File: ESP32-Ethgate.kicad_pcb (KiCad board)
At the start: 2 copper layers, 58 parts, among them J1 USB_B_Micro, J2 RJ45_Amphenol_RJMG1BD3B8K1ANR, Q1 UMH3N, SW1 RESET, SW2 PROG, U1 AMS1117-3.3, U2 ESP32-WROOM-32U, U3 CH340C, U4 W5500, Y1 25MHz

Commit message: finished layout
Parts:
- removed C17: 22n, Capacitor_SMD:C_0603_1608Metric
- removed C18, C19, C20, C21, C22, C23: 100n, Capacitor_SMD:C_0603_1608Metric
- removed R4: 0R, Resistor_SMD:R_0603_1608Metric
- removed SW1: RESET, Button_Switch_SMD:SW_SPST_CK_RS282G05A3
- removed SW2: PROG, Button_Switch_SMD:SW_SPST_CK_RS282G05A3
- removed Y1: 25MHz, Crystal:Crystal_SMD_3225-4Pin_3.2x2.5mm_HandSoldering
- added R22: 49K9, Resistor_SMD:R_0603_1608Metric, B.Cu at (90.9, 90.9)
- added R23: 0R, Resistor_SMD:R_0603_1608Metric, B.Cu at (74.0, 75.9)
- added R8: 10K, Resistor_SMD:R_0603_1608Metric, B.Cu at (108.8, 96.5)
- added U5: LAN8720A, Package_DFN_QFN:QFN-24-1EP_4x4mm_P0.5mm_EP2.6x2.6mm, B.Cu at (107.3, 88.0)
- C1, C2: value 100nF -> 100n; moved to B.Cu
- C10: value 22u -> 100n; footprint Capacitor_SMD:C_0805_2012Metric -> Capacitor_SMD:C_0603_1608Metric; moved to B.Cu
- C11: value 100n -> 1u1R; moved to B.Cu
- C12: value 4.7u -> 10n; footprint Capacitor_SMD:C_0805_2012Metric -> Capacitor_SMD:C_0603_1608Metric; moved to B.Cu
- C13: value 10n -> 470p; moved to B.Cu
- C14: value 10n -> 22n; moved to B.Cu
- C15: value 6.8n -> 10n; moved to B.Cu
- C16: value 6.8n -> 22n; moved to B.Cu
- C3, C4, C5, C6, C7, D1, F1, Q1, R1, R17, R18, R2, R5, U1, U3: moved to B.Cu
- C8, C9: value 18p -> 100n; moved to B.Cu
- FB1: value 120R@100MHz -> 30R; footprint Inductor_SMD:L_0603_1608Metric_Pad1.05x0.95mm_HandSolder -> Inductor_SMD:L_0603_1608Metric; moved to B.Cu
- J2: value RJ45_Amphenol_RJMG1BD3B8K1ANR -> HR911105A; footprint Connector_RJ:RJ45_Amphenol_RJMG1BD3B8K1ANR -> Connector_RJ:RJ45_Hanrun_HR911105A
- R10: value 10K -> 1K5; moved to B.Cu
- R11, R14: value 49R9 -> 10R; moved to B.Cu
- R12, R15: value 49R9 -> 33R; moved to B.Cu
- R13: value 12K4 1% -> 33R; moved to B.Cu
- R16, R20, R21: value 10K -> 49K9; moved to B.Cu
- R19: value 0R -> 12K1; moved to B.Cu
- R6: value 1M -> 10R; moved to B.Cu
- R9: value 10K -> 10R; moved to B.Cu
- U4: value W5500 -> 50MHz; footprint Package_QFP:LQFP-48_7x7mm_P0.5mm -> Oscillator:Oscillator_SMD_Abracon_ASDMB-4Pin_2.5x2.0mm; moved to B.Cu
- moved R3 110.1 mm to (74.1, 77.5)
- moved R21 108.2 mm to (90.9, 83.4), turned to 180 degrees
- moved R17 105.6 mm to (90.9, 93.1), turned to 180 degrees
- moved R18 104.9 mm to (90.9, 94.7), turned to 180 degrees
- moved R20 104.7 mm to (90.9, 86.5), turned to 180 degrees
- moved D2 102.0 mm to (69.8, 77.5)
- moved D3 101.4 mm to (70.1, 62.9)
- moved C3 96.5 mm to (85.2, 65.0), turned to 90 degrees
- moved R16 95.9 mm to (90.9, 88.3), turned to 180 degrees
- moved C16 93.9 mm to (90.9, 81.5)
- moved R7 91.8 mm to (74.5, 63.5)
- moved C4 91.0 mm to (98.7, 73.8), turned to 270 degrees
- moved C15 89.1 mm to (105.5, 96.5), turned to 270 degrees
- moved C7 88.6 mm to (100.3, 63.4), turned to 180 degrees
- moved C6 88.1 mm to (91.1, 76.5)
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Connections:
- net SLED renamed /SLED
- C1 pad 1: +3V3 -> GND
- C1 pad 2: GND -> +3V3
- C11 pad 1: +3V3 -> /VDDCR
- C12 pad 1: GND -> +3.3VA
- C12 pad 2: Net-(C12-Pad2) -> GND
- C13 pad 1: GND -> /VDDCR
- C13 pad 2: Net-(C13-Pad2) -> GND
- C14 pad 1: Net-(C14-Pad1) -> +3.3VA
- C15 pad 1: Net-(C15-Pad1) -> +3.3VA
- C15 pad 2: /RXN -> GND
- C16 pad 1: Net-(C16-Pad1) -> +3.3VA
- C16 pad 2: /RXP -> GND
- C2 pad 1: +3V3 -> /EN
- C8 pad 1: /XI -> +3V3
- C9 pad 1: /XO -> /nRST
- J1 pad 6: Net-(J1-Pad6) -> GND1
- R10 pad 1: Net-(R10-Pad1) -> +3V3
- R10 pad 2: +3V3 -> /MDIO
- R11 pad 1: +3.3VA -> /CRS_DV
- R11 pad 2: /TXP -> Net-(R11-Pad2)
- R12 pad 1: /RXN -> /IO0
- R12 pad 2: Net-(C14-Pad1) -> Net-(R12-Pad2)
- R13 pad 1: GND -> /IO0
- R13 pad 2: Net-(R13-Pad2) -> /CLOCK
- R14 pad 1: +3.3VA -> Net-(R14-Pad1)
- R14 pad 2: /TXP -> /RXD0
- R15 pad 1: /RXP -> /CLOCK
- R15 pad 2: Net-(C14-Pad1) -> /XTAL
- R16 pad 1: +3.3VA -> /RXP
- R16 pad 2: Net-(C17-Pad1) -> +3.3VA
- R17 pad 2: Net-(J2-PadL2) -> Net-(J2-Pad9)
- R18 pad 2: Net-(J2-PadL3) -> Net-(J2-Pad11)
- R19 pad 1: Net-(J2-Pad13) -> GND
- R19 pad 2: GND -> /RBIAS
- R20 pad 1: +3V3 -> /TXN
- R20 pad 2: /~SCS -> +3.3VA
- R21 pad 1: +3V3 -> /TXP
- R21 pad 2: /~WRST -> +3.3VA
- R5 pad 1: Net-(R5-Pad1) -> /PHY_PWR
- R5 pad 2: +3V3 -> GND
- R6 pad 1: /XO -> Net-(R6-Pad1)
- R6 pad 2: /XI -> +3V3
- R9 pad 2: +3V3 -> /RXD1
- U2 pad 10: /EN -> /RXD0
- U2 pad 11: /~WRST -> /RXD1
- U2 pad 12: (no net) -> /CRS_DV
- U2 pad 28: (no net) -> /PHY_PWR
- U2 pad 29: /~SCS -> (no net)
- U2 pad 30: /SCLK -> /MDIO
- U2 pad 31: /MISO -> /TXD0
- U2 pad 33: (no net) -> /TXEN
- U2 pad 36: (no net) -> /TXD1
- U2 pad 37: /MOSI -> /MDC
- U4 pad 1: /TXN -> /PHY_PWR
- U4 pad 2: /TXP -> GND
- U4 pad 3: GND -> /CLOCK
- U4 pad 4: +3.3VA -> +3V3
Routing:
- net +3V3: track 0.00 -> 163.0 mm, vias 0 -> 9
- net +3.3VA: track 0.00 -> 82.4 mm, vias 0 -> 7
- net /SLED: track 0.00 -> 65.6 mm, vias 0 -> 4
- net /eRX: track 0.00 -> 58.8 mm, vias 0 -> 1
- net /TXD1: track 0.00 -> 47.7 mm, vias 0 -> 3
- net /eTX: track 0.00 -> 46.6 mm, vias 0 -> 1
- net /TXEN: track 0.00 -> 39.8 mm, vias 0 -> 1
- net /TXD0: track 0.00 -> 39.3 mm, vias 0 -> 1
- net /MDC: track 0.00 -> 38.7 mm, vias 0 -> 1
- net Net-(J1-Pad2): track 0.00 -> 37.0 mm, vias 0 -> 1
- net /EN: track 0.00 -> 36.9 mm, vias 0 -> 2
- net Net-(J1-Pad3): track 0.00 -> 34.9 mm, vias 0 -> 1
- net /PHY_PWR: track 0.00 -> 34.9 mm, vias 0 -> 1
- net /IO0: track 0.00 -> 33.2 mm, vias 0 -> 1
- net +5V: track 0.00 -> 29.7 mm
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- added copper zone on B.Cu, net GND
- added copper zone on F.Cu, net GND
- added copper zone on B.Cu, net GND1
- added copper zone on F.Cu, net GND1
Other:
- board outline added: 76.2 x 38.1 mm
- net class Default: clearance 0.3 -> 0.26; via_dia 1.2 -> 1
- rule trace_clearance: 0.3 -> 0.26
- rule via_min_size: 1.2 -> 1
- board text added: "ESP32-Ethgate v1 cperiod 2021"

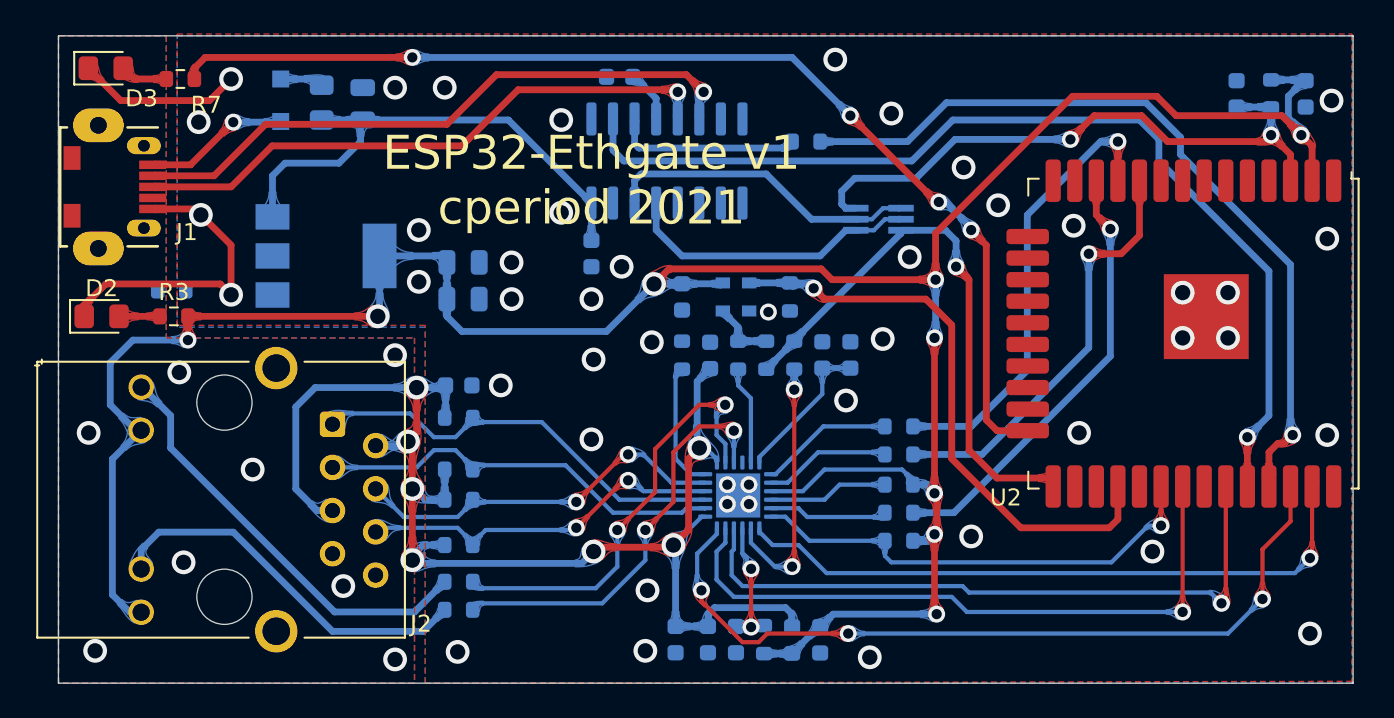
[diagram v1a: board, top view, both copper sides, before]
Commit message: add USB ESD, generate rounded tracks version
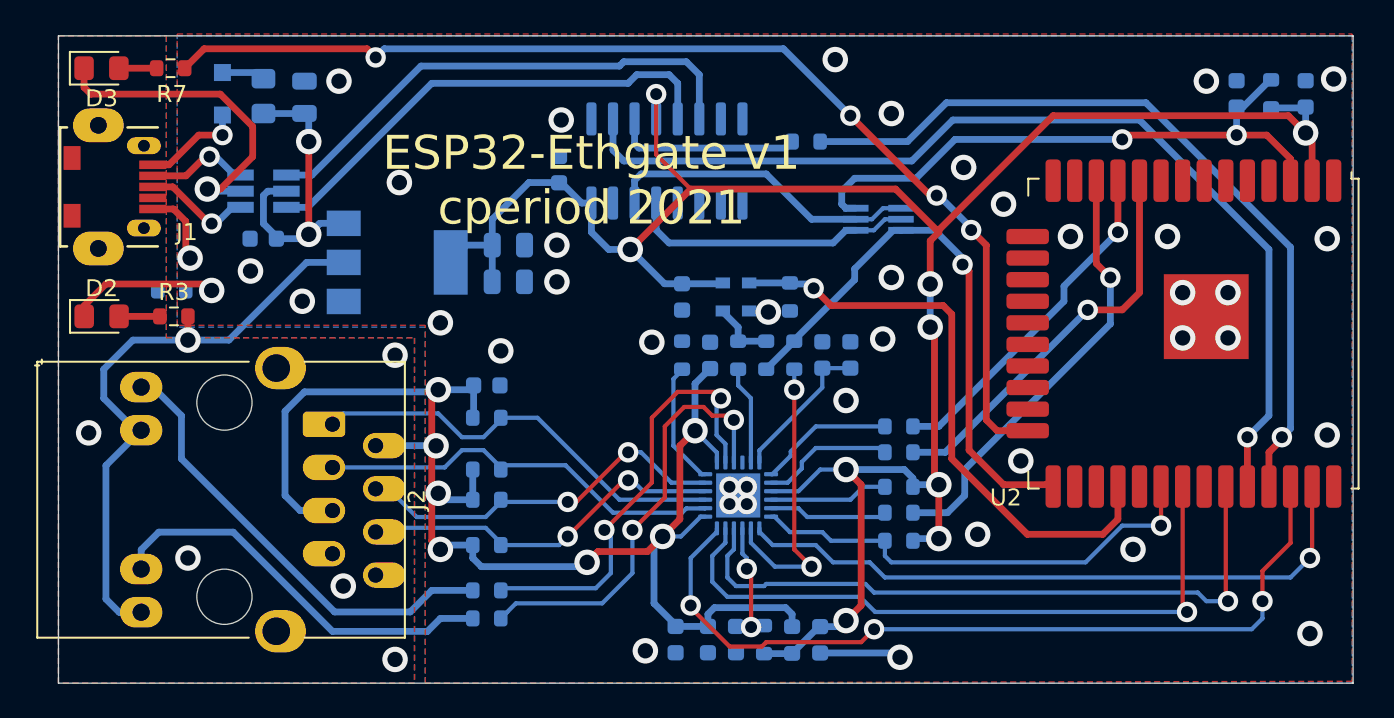
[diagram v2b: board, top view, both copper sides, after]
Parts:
- added U6: USBLC6-2SC6, Package_TO_SOT_SMD:SOT-23-6_Handsoldering, B.Cu at (79.4, 70.1)
- J2: footprint Connector_RJ:RJ45_Hanrun_HR911105A -> CPB:RJ45_Hanrun_HR911105A_Oval
- moved C7 23.0 mm to (79.4, 72.9)
- moved C4 5.29 mm to (96.8, 68.8), turned to 90 degrees
- moved U1 4.21 mm to (87.2, 74.3)
- moved C3 3.45 mm to (81.8, 64.6)
- moved D1 3.45 mm to (77.0, 64.4)
- moved F1 3.45 mm to (79.4, 64.5)
- moved C5 2.85 mm to (93.8, 73.3)
- moved C6 2.85 mm to (93.8, 75.4)
- moved R18 1.73 mm to (92.5, 95.2)
- moved R17 1.73 mm to (92.5, 93.6)
- moved C16 1.65 mm to (92.5, 81.5)
- moved R16 1.65 mm to (92.5, 88.3)
- moved R20 1.65 mm to (92.5, 86.5)
- moved R21 1.65 mm to (92.5, 83.4)
- moved R22 1.65 mm to (92.5, 90.9)
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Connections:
- C4 pad 1: +5V -> +3V3
- C7 pad 1: Net-(C7-Pad1) -> +5V
- U3 pad 16: +5V -> +3V3
- U3 pad 4: Net-(C7-Pad1) -> +3V3
- U3 pad 5: Net-(J1-Pad3) -> Net-(U3-Pad5)
- U3 pad 6: Net-(J1-Pad2) -> Net-(U3-Pad6)
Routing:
- net Net-(J1-Pad2): track 37.0 -> 6.19 mm
- net Net-(U3-Pad6): track 0.00 -> 30.0 mm
- net Net-(U3-Pad5): track 0.00 -> 28.6 mm
- net Net-(J1-Pad3): track 34.9 -> 6.51 mm
- net +5V: track 29.7 -> 19.2 mm, vias 0 -> 2
- net GND: track 28.2 -> 37.4 mm, vias 46 -> 41
- net /RXD1: track 27.2 -> 19.9 mm
- net +3V3: track 163.0 -> 167.7 mm, vias 9 -> 10
- net +3.3VA: track 82.4 -> 85.5 mm
- net Net-(C7-Pad1): track 3.11 -> 0.00 mm
- net Net-(D1-Pad2): track 8.59 -> 6.01 mm
- net Net-(J2-Pad9): track 25.2 -> 27.0 mm
- net /TXD1: track 47.7 -> 49.5 mm
- net /ACTLED: track 24.6 -> 26.2 mm
- net Net-(R12-Pad2): track 15.5 -> 17.0 mm
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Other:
- net class Default: via_dia 1 -> 1.2; via_drill 0.6 -> 0.7
- net class Power added: clearance 0.3, trace_width 0.4, via_dia 1.5, via_drill 0.9
- rule via_min_drill: 0.6 -> 0.7
- rule via_min_size: 1 -> 1.2

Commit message: more tweaks
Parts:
- R16, R20, R21, R22: value 49K9 -> 49R9
- R17, R18, R3, R7: value 1K -> 1K5

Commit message: better, but still not working.
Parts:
- added D4: GREEN, LED_SMD:LED_0603_1608Metric_Castellated, F.Cu at (89.7, 80.2)
- added R4: 10K, Resistor_SMD:R_0603_1608Metric, F.Cu at (98.8, 74.9)
- C1, C10, C11, C12, C13, C14, C15, C16, C2, C3, C4, C5, C6, C7, C9, D1, F1, FB1, Q1, R1, R10, R11, R14, R15, R16, R17, R18, R19, R2, R20, R21, R22, R23, R8, R9, U3, U5, U6: moved to F.Cu
- C8: value 100n -> 22u; footprint Capacitor_SMD:C_0603_1608Metric -> Capacitor_SMD:C_0805_2012Metric; moved to F.Cu
- D2, D3: footprint LED_SMD:LED_0805_2012Metric_Pad1.15x1.40mm_HandSolder -> LED_SMD:LED_0603_1608Metric_Castellated
- R12: value 33R -> 10K; moved to F.Cu
- R13: value 33R -> 1K5; moved to F.Cu
- R5: value 10K -> 1K5; moved to F.Cu
- R6: value 10R -> 1K5; moved to F.Cu
- U1: value AMS1117-3.3 -> HT7233; footprint Package_TO_SOT_SMD:SOT-223-3_TabPin2 -> Package_TO_SOT_SMD:SOT-23-5; moved to F.Cu
- U4: value 50MHz -> HT7233; footprint Oscillator:Oscillator_SMD_Abracon_ASDMB-4Pin_2.5x2.0mm -> Package_TO_SOT_SMD:SOT-23-5; moved to F.Cu
- moved R1 24.1 mm to (115.8, 71.8), turned to 0 degrees
- moved FB1 18.9 mm to (96.0, 84.4), turned to 270 degrees
- moved C10 18.3 mm to (105.3, 79.5), turned to 90 degrees
- moved R5 17.7 mm to (93.1, 80.2), turned to 0 degrees
- moved C9 17.0 mm to (106.9, 79.5), turned to 90 degrees
- moved R8 17.0 mm to (108.6, 79.5), turned to 90 degrees
- moved C11 15.8 mm to (110.1, 95.4), turned to 270 degrees
- moved C13 15.8 mm to (111.8, 95.4), turned to 270 degrees
- moved R15 15.6 mm to (107.8, 95.3), turned to 90 degrees
- moved C12 15.5 mm to (104.8, 95.3), turned to 270 degrees
- moved R19 15.5 mm to (103.1, 95.2), turned to 90 degrees
- moved C15 14.4 mm to (97.7, 84.4), turned to 90 degrees
- moved C14 12.8 mm to (99.4, 84.4), turned to 90 degrees
- moved C3 10.6 mm to (82.3, 75.1)
- moved D1 10.6 mm to (77.5, 74.9), turned to 90 degrees
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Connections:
- C10 pad 1: +3V3 -> /+3V3_LAN
- C8 pad 1: +3V3 -> /+3V3_LAN
- FB1 pad 1: +3V3 -> /+3V3_LAN
- J2 pad 10: +3V3 -> /+3V3_LAN
- J2 pad 12: +3V3 -> /+3V3_LAN
- R10 pad 1: +3V3 -> /+3V3_LAN
- R12 pad 1: /IO0 -> /+3V3_LAN
- R13 pad 1: /IO0 -> /+3V3_LAN
- R13 pad 2: /CLOCK -> /CRS_DV
- R15 pad 1: /CLOCK -> /PHY_CLK
- R5 pad 1: /PHY_PWR -> Net-(D4-Pad2)
- R5 pad 2: GND -> /+3V3_LAN
- R6 pad 2: +3V3 -> /+3V3_LAN
- R8 pad 2: +3V3 -> /+3V3_LAN
- U1 pad 1: GND -> +5V
- U1 pad 2: +3V3 -> GND
- U2 pad 14: (no net) -> /PHY_POWER
- U2 pad 28: /PHY_PWR -> /PHY_CLK
- U4 pad 1: /PHY_PWR -> +5V
- U4 pad 3: /CLOCK -> /PHY_POWER
- U4 pad 4: +3V3 -> (no net)
- U5 pad 9: +3V3 -> /+3V3_LAN
- U6 pad 1: Net-(J1-Pad3) -> Net-(J1-Pad2)
- U6 pad 3: Net-(J1-Pad2) -> Net-(J1-Pad3)
- U6 pad 4: Net-(U3-Pad6) -> Net-(U3-Pad5)
- U6 pad 6: Net-(U3-Pad5) -> Net-(U3-Pad6)
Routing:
- net /+3V3_LAN: track 0.00 -> 92.6 mm, vias 0 -> 5
- net +3V3: track 167.7 -> 109.5 mm, vias 10 -> 9
- net /PHY_POWER: track 0.00 -> 36.3 mm, vias 0 -> 2
- net /PHY_PWR: track 35.6 -> 0.00 mm, vias 1 -> 0
- net /PHY_CLK: track 0.00 -> 28.5 mm
- net Net-(U3-Pad6): track 30.0 -> 7.69 mm
- net Net-(U3-Pad5): track 28.6 -> 9.63 mm
- net +5V: track 19.2 -> 37.9 mm
- net GND: track 37.4 -> 55.5 mm, vias 41 -> 42
- net +3.3VA: track 85.5 -> 73.6 mm, vias 7 -> 4
- net /RXD1: track 19.9 -> 30.8 mm, vias 1 -> 2
- net /LINKLED: track 26.3 -> 15.9 mm
- net Net-(R12-Pad2): track 17.0 -> 6.65 mm, vias 2 -> 0
- net /TXN: track 24.3 -> 33.9 mm
- net /ACTLED: track 26.2 -> 17.7 mm
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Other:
- board text added: "ESP32-Ethgate v2 cperiod 2021"
- board text removed: "ESP32-Ethgate v1 cperiod 2021"

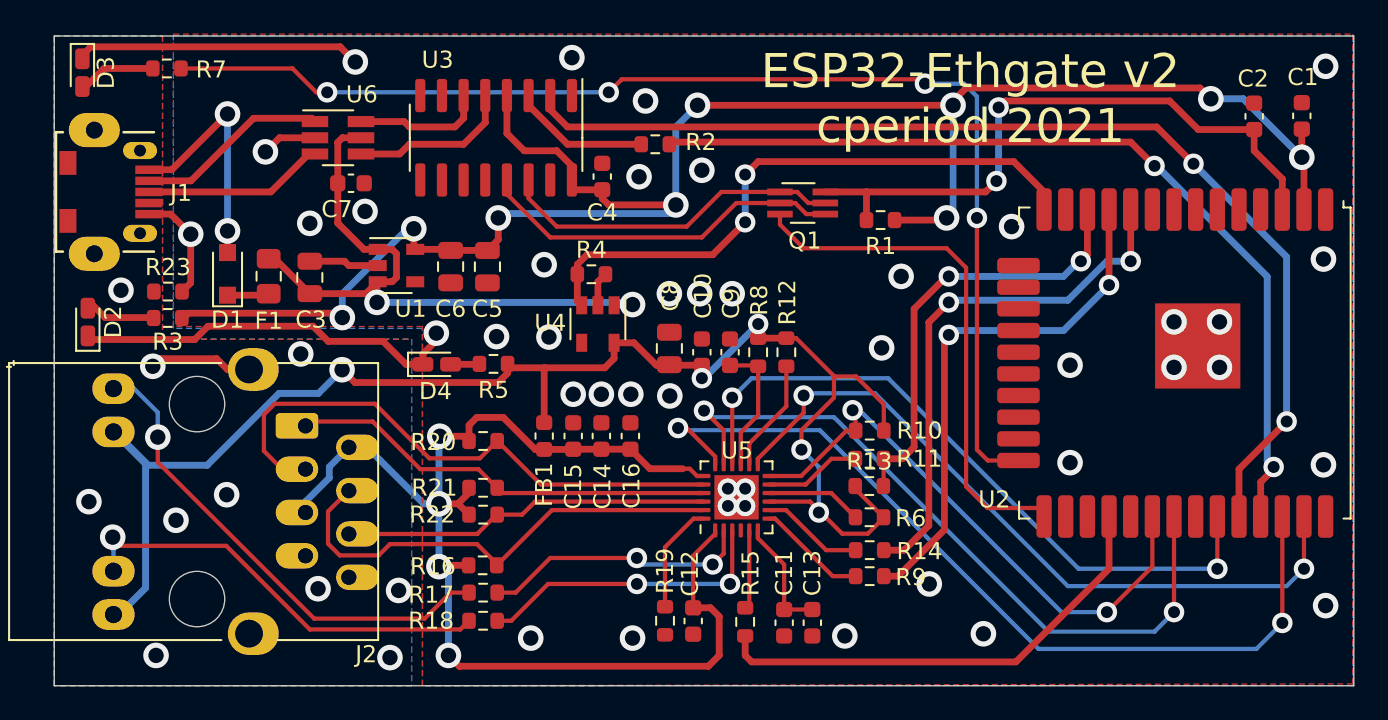
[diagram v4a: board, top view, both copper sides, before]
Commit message: some layout tweaks to clean things up and make assembly a hair easier
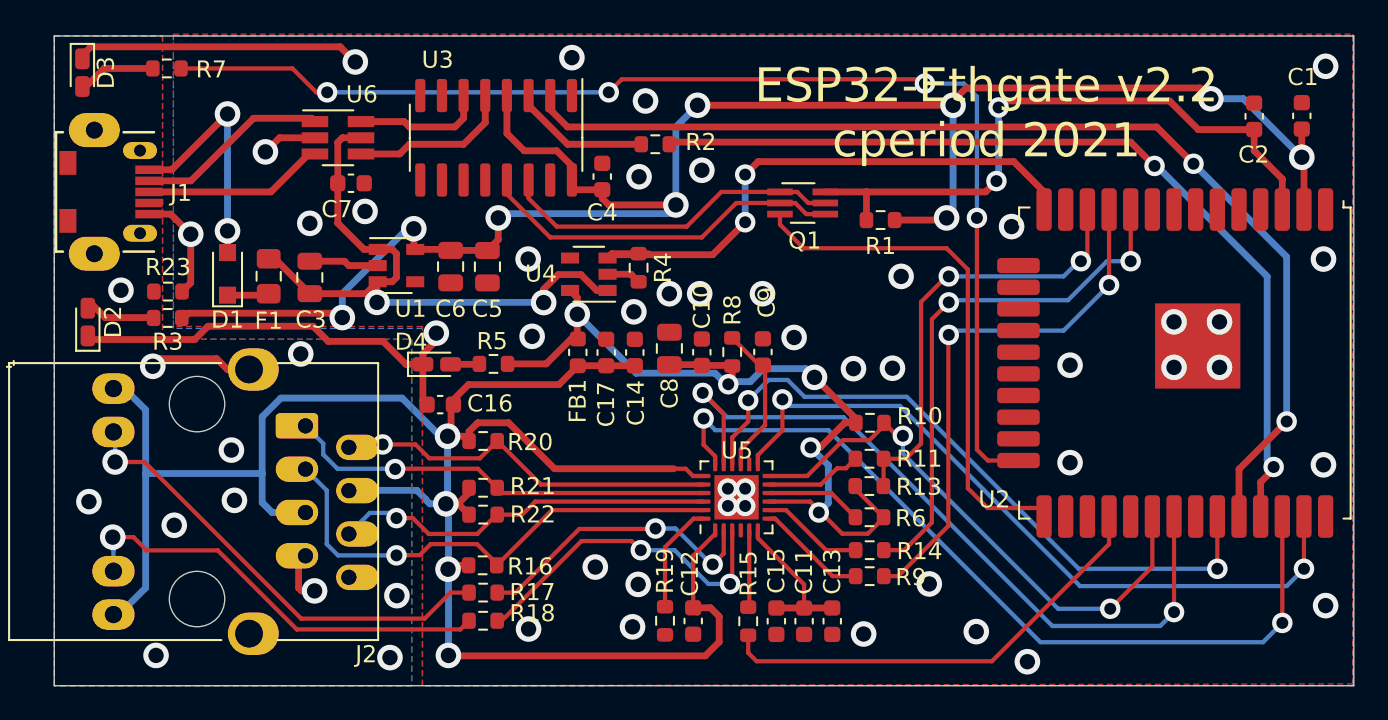
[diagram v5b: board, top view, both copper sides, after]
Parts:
- removed R12: 10K, Resistor_SMD:R_0603_1608Metric
- added C17: 100n, Capacitor_SMD:C_0603_1608Metric, F.Cu at (99.7, 79.5)
- R6: value 1K5 -> 10R
- moved C15 16.1 mm to (109.7, 95.3), turned to 270 degrees
- moved C16 11.3 mm to (89.9, 82.6), turned to 180 degrees
- moved FB1 5.29 mm to (98.0, 79.5)
- moved C14 5.28 mm to (101.4, 79.5)
- moved U4 2.97 mm to (98.7, 74.9), turned to 180 degrees
- moved R4 2.79 mm to (101.6, 74.5), turned to 270 degrees
- moved C9 1.93 mm to (108.9, 79.5), turned to 270 degrees
- moved R8 1.52 mm to (107.1, 79.5)
- moved C11 1.17 mm to (111.3, 95.3)
- moved C13 1.17 mm to (112.9, 95.3)
- moved R10 0.46 mm to (115.1, 83.6), turned to 0 degrees
- moved R15 0.18 mm to (108.0, 95.3), turned to 270 degrees
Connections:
- C15 pad 1: +3.3VA -> /VDDCR
- C9 pad 1: /nRST -> GND
- C9 pad 2: GND -> /nRST
- J2 pad 10: /+3V3_LAN -> Net-(J2-Pad10)
- J2 pad 12: /+3V3_LAN -> +3.3VA
- J2 pad 2: +3.3VA -> /TXN
- J2 pad 3: /TXN -> /RXP
- J2 pad 4: /RXP -> +3.3VA
- J2 pad 7: (no net) -> GND1
- J2 pad 9: Net-(J2-Pad9) -> +3.3VA
- R15 pad 1: /PHY_CLK -> /XTAL
- R15 pad 2: /XTAL -> /PHY_CLK
- R17 pad 2: Net-(J2-Pad9) -> Net-(J2-Pad10)
- R8 pad 1: /nRST -> /+3V3_LAN
- R8 pad 2: /+3V3_LAN -> /nRST
- U5 pad 14: Net-(R12-Pad2) -> (no net)
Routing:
- net +3.3VA: track 73.6 -> 121.2 mm
- net /+3V3_LAN: track 92.6 -> 51.0 mm
- net Net-(J2-Pad9): track 28.8 -> 0.00 mm, vias 1 -> 0
- net Net-(J2-Pad10): track 0.00 -> 27.0 mm, vias 0 -> 1
- net /TXN: track 33.9 -> 22.7 mm, vias 0 -> 1
- net Net-(R12-Pad2): track 6.65 -> 0.00 mm
- net GND1: track 6.09 -> 9.15 mm, vias 10 -> 11
- net GND: track 55.5 -> 58.0 mm, vias 42 -> 43
- net /ACTLED: track 17.7 -> 19.8 mm
- net /VDDCR: track 6.93 -> 8.99 mm
- net /TXD1: track 51.5 -> 49.5 mm
- net /PHY_POWER: track 36.3 -> 34.3 mm
- net /LINKLED: track 15.9 -> 17.3 mm
- net /RXP: track 28.1 -> 29.5 mm, vias 0 -> 1
- net /TXD0: track 43.1 -> 44.4 mm
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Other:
- board text added: "ESP32-Ethgate v2.2 cperiod 2021"
- board text removed: "ESP32-Ethgate v2 cperiod 2021"
